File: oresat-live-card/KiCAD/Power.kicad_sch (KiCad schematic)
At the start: 120 parts, among them Q2 PMV45EN2R, Q3 DMP2240UDM, Q4 PMV45EN2R, Q5 DMP3050LVT-7, Q6 DMP3050LVT-7, U12 MIC842LYC5, U13 MIC842LYC5, U14 MAX4211FETE, U15 LTC3624-5, U16 MAX7310ATE, U21 TLV733P-Q1, U22 TS5A21366, U5 LTC3624-5

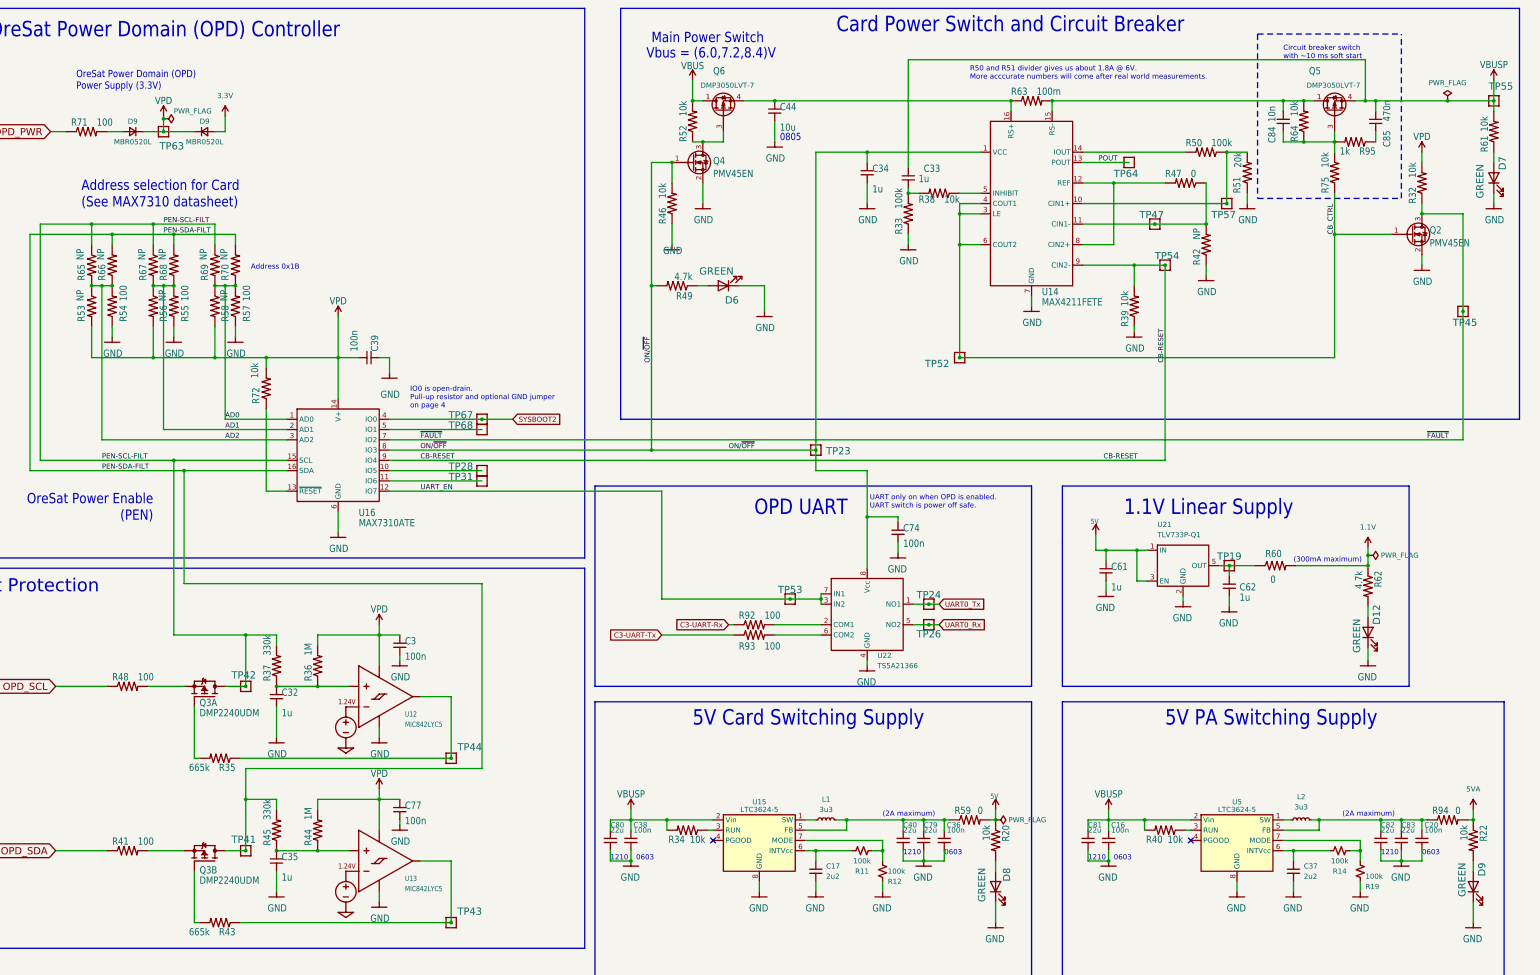
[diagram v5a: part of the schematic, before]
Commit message: Upgraded to KiCAD 8.0. Added notes on U.FL cable and USB cables to wifi and camera.
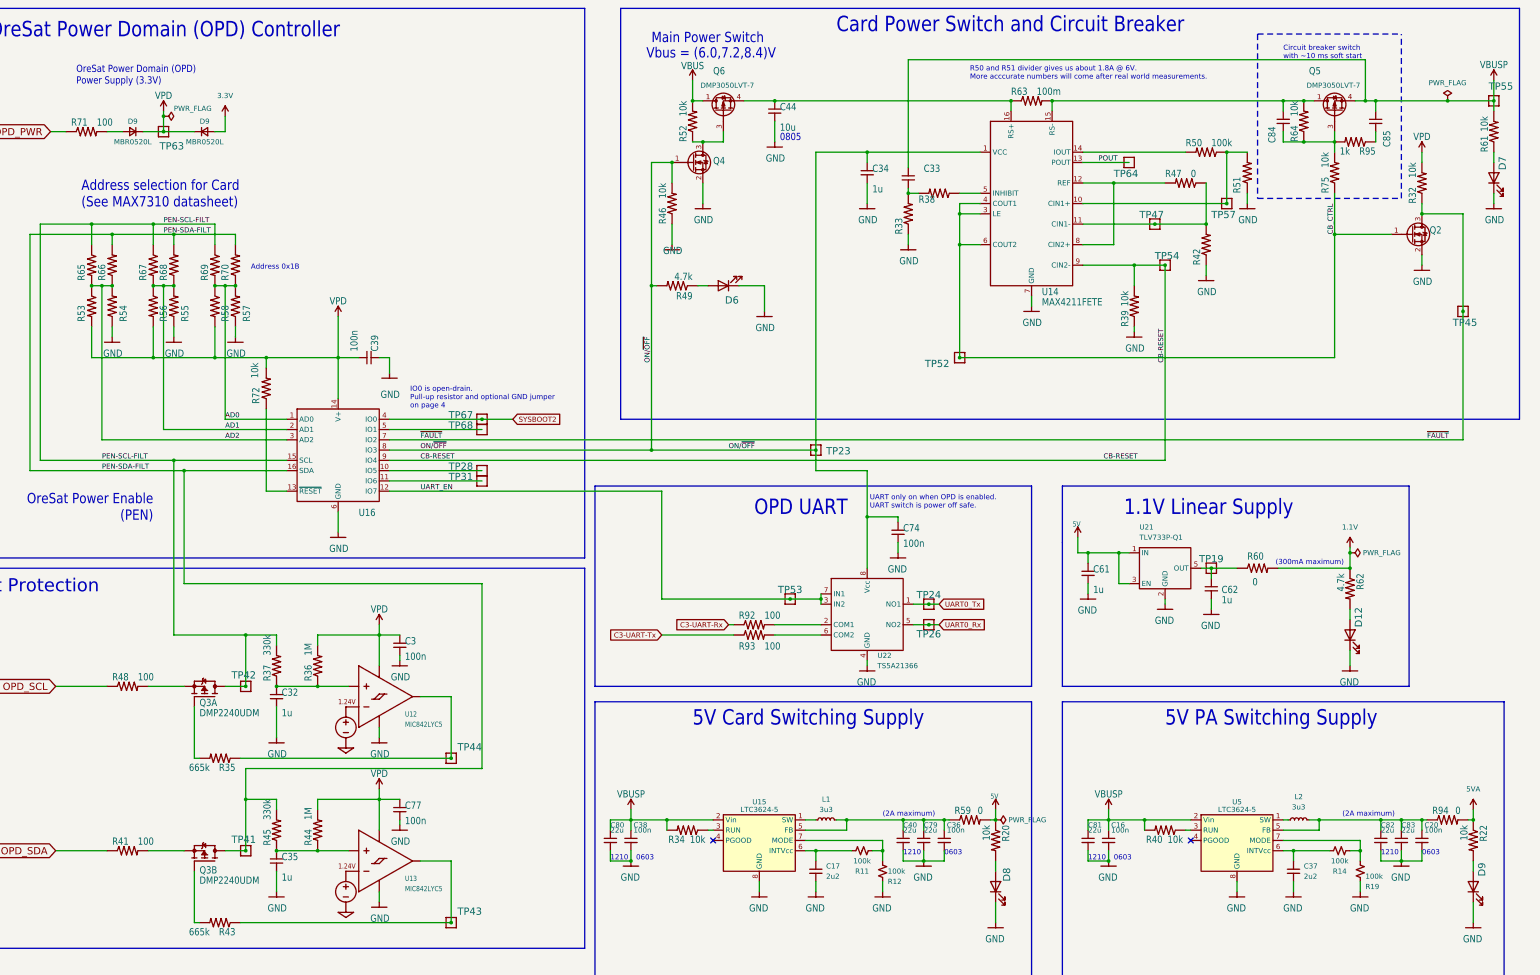
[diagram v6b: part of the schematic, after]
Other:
- moved on the sheet: C61, C62, D12, L2, R60, R62, TP19, U21

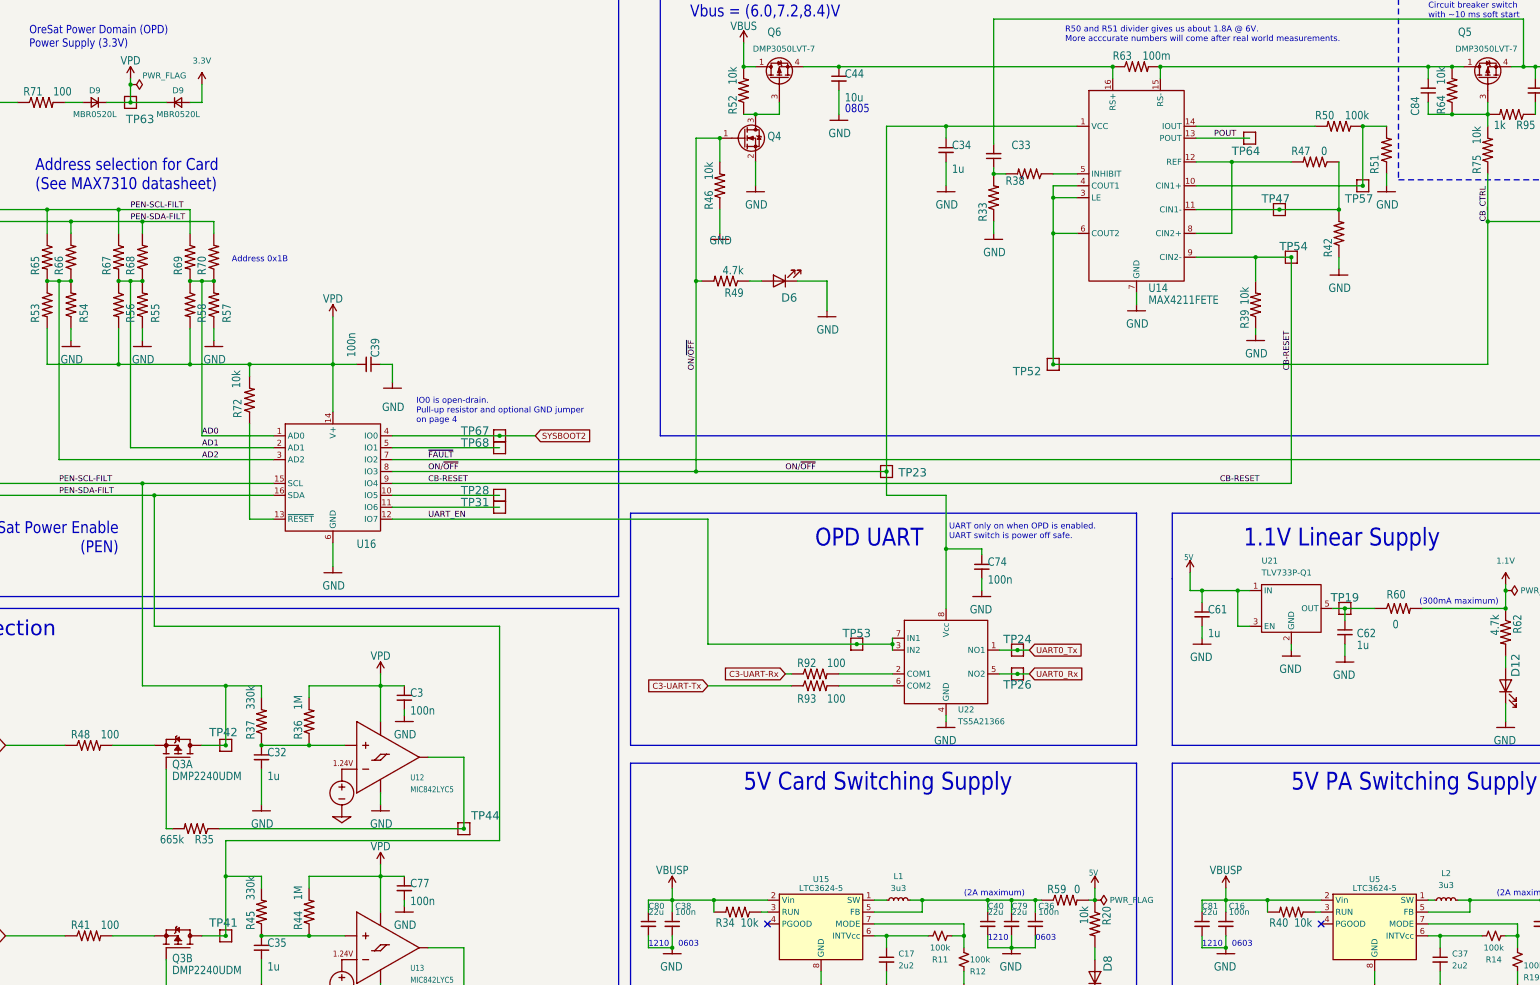
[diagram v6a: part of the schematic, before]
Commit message: added new sheets for LNA and switching
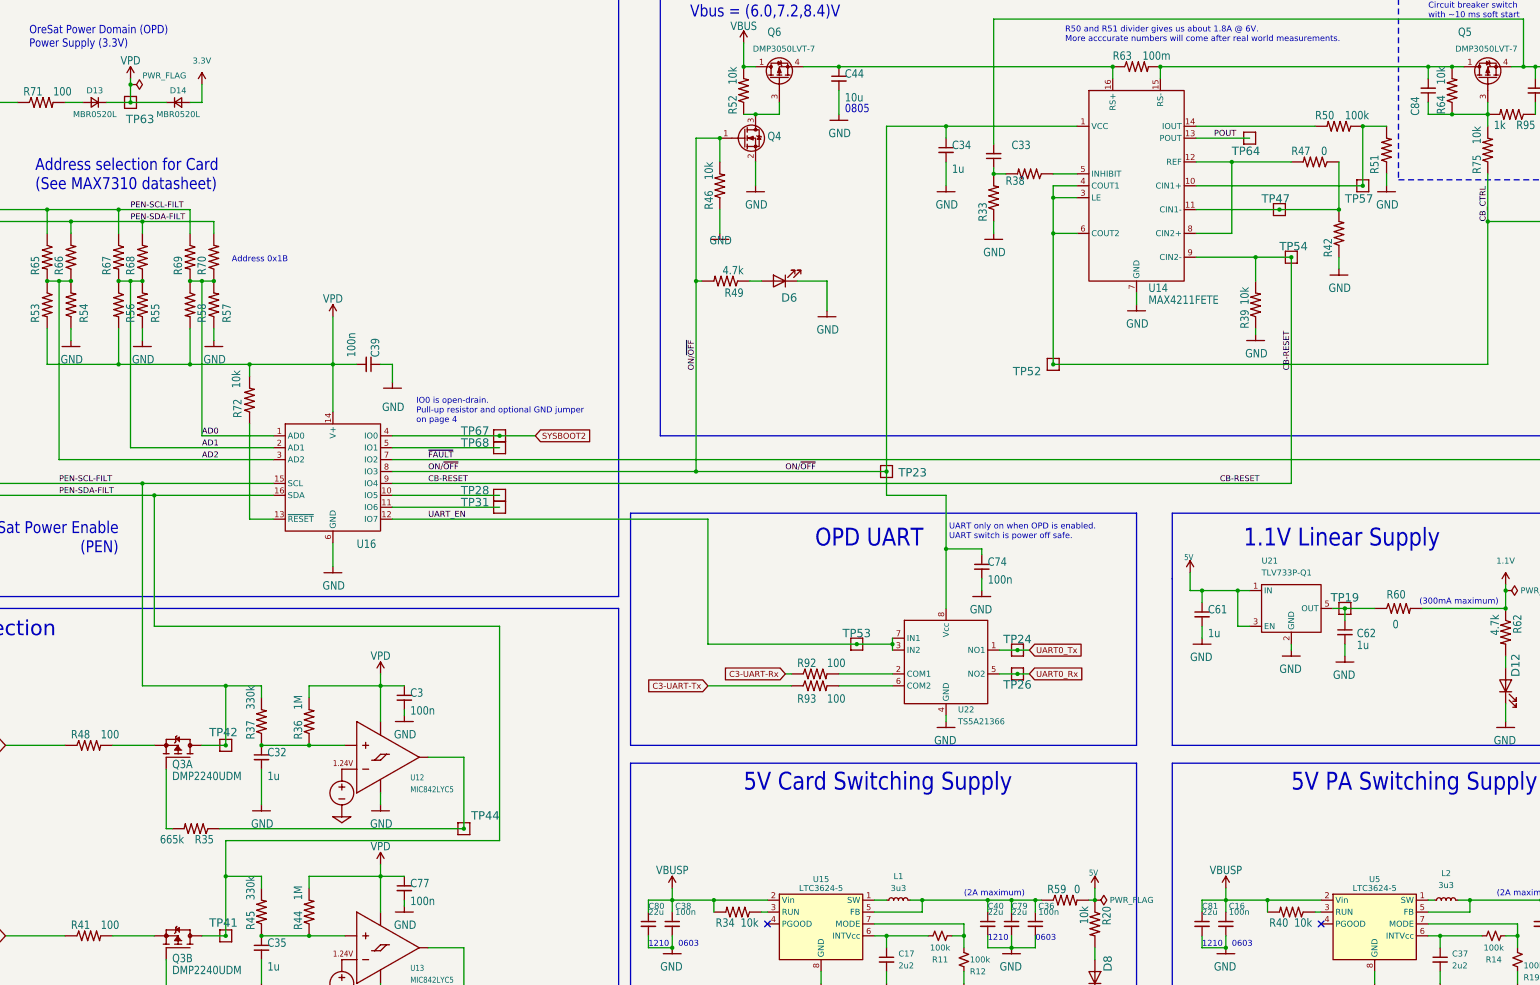
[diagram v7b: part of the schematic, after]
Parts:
- renumbered D9 to D13, D9 to D14

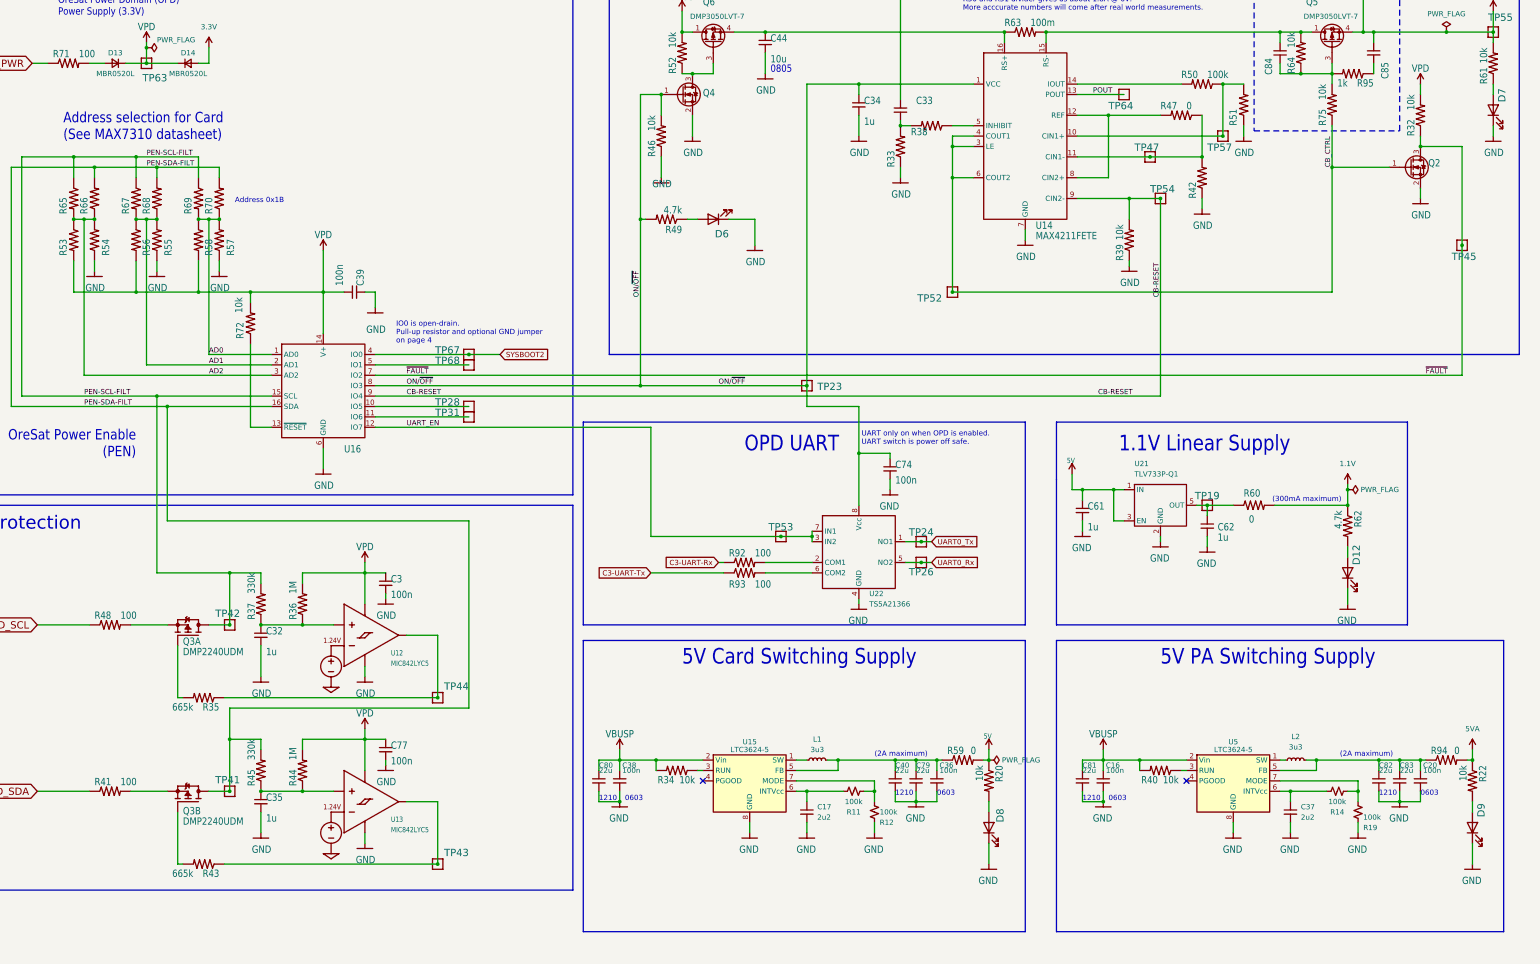
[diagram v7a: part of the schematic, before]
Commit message: completed tx/rx switch circuit and cleaned up GND references
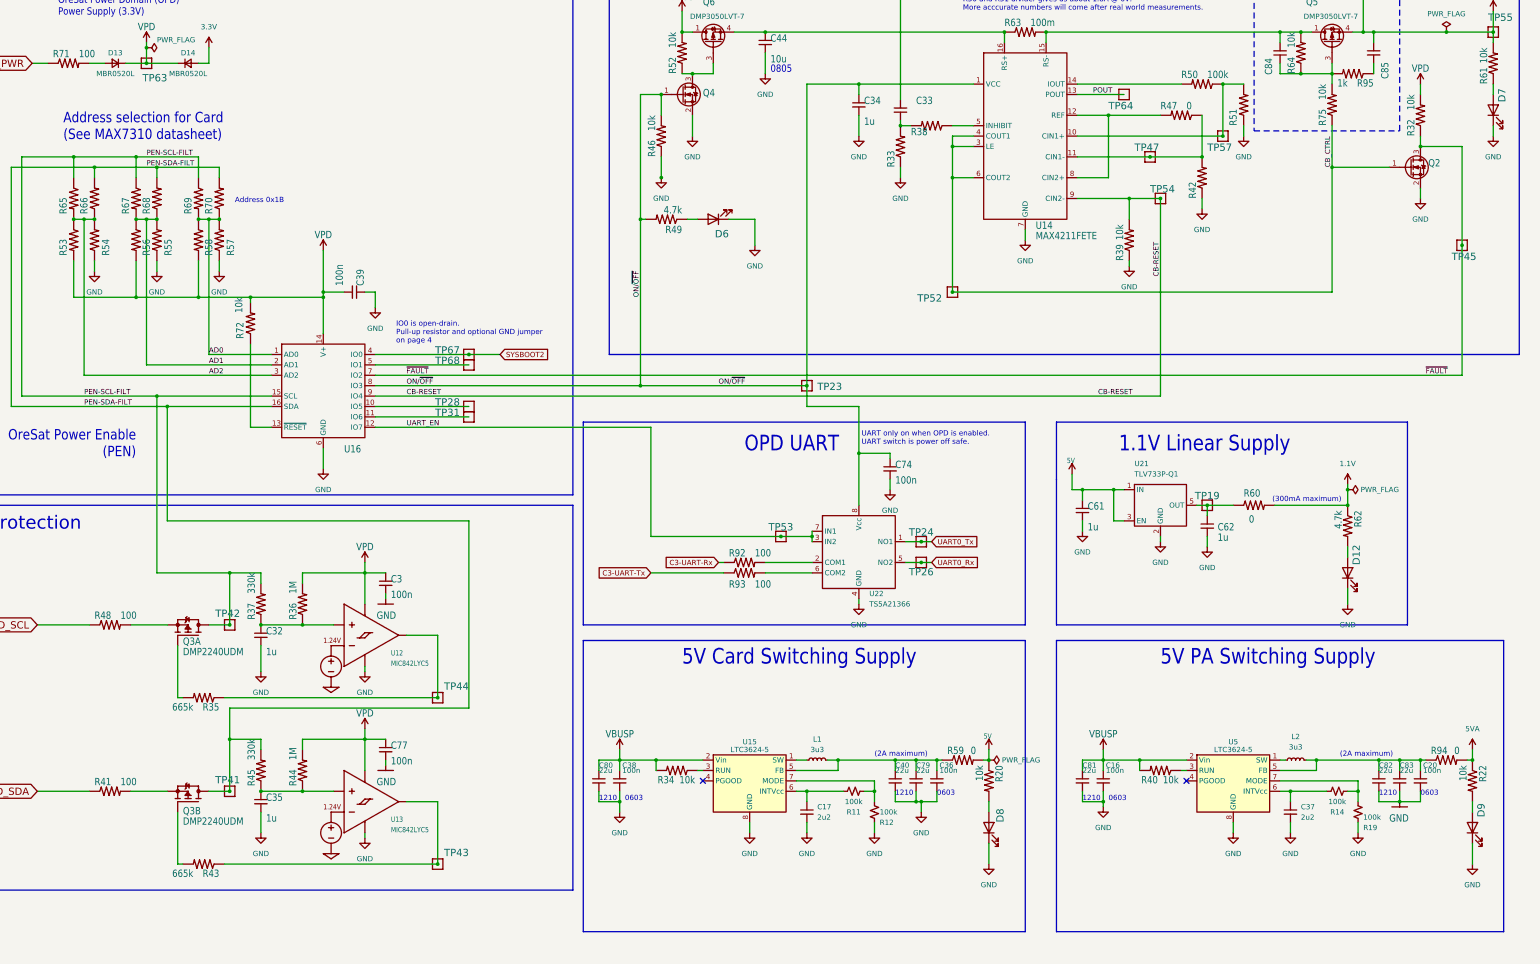
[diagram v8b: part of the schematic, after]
